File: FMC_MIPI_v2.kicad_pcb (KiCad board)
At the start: 6 copper layers, 69 x 112 mm, 67 parts, among them IC1 ECLAMP2398P.TCT, IC2 AT24MAC402-MAHM-T, J1 ASP-134488-01, J2 QTH-060-01-L-D-A, U2 SN74AVC2T45DCUR, U5 TS3DDR3812_RUA_42, U6 TS3DDR3812_RUA_42, U8 SN74AVCH16T245_DGV_48

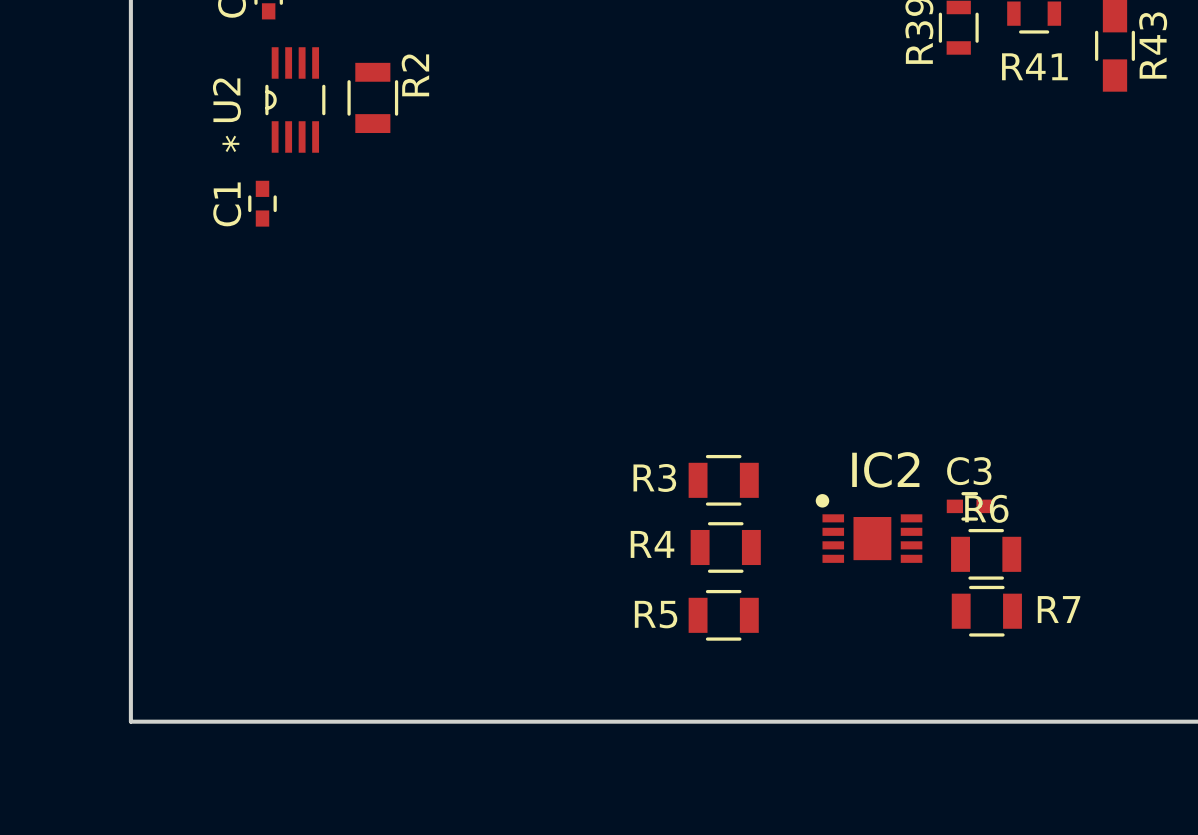
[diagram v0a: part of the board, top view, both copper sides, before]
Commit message: added more level shifters and power 1.8 Volt
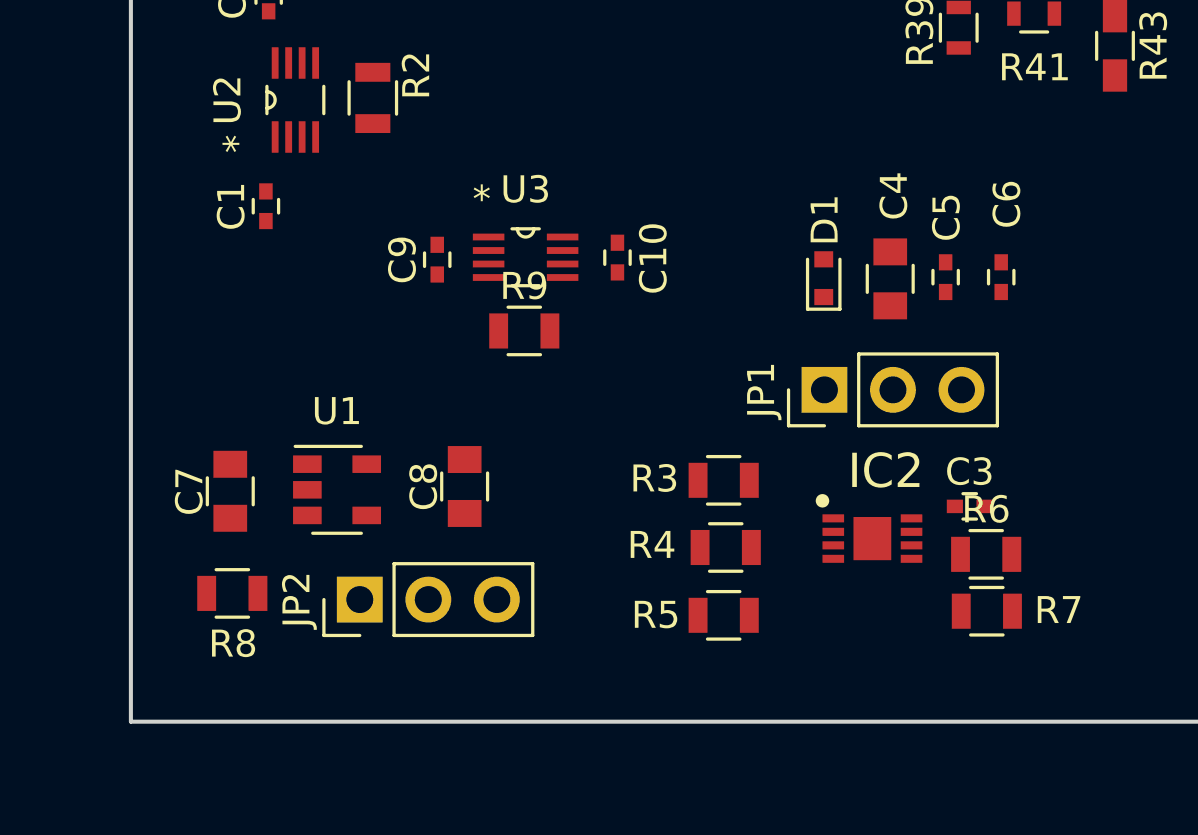
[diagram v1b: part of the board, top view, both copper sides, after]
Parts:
- added C10: 0.1uF, Capacitors_SMD:C_0402, F.Cu at (108.5, 123.8)
- added C4: 4.7uF, Capacitors_SMD:C_0805, F.Cu at (118.6, 124.6)
- added C5: 0.1uF, Capacitors_SMD:C_0402, F.Cu at (120.7, 124.5)
- added C6: 0.1uF, Capacitors_SMD:C_0402, F.Cu at (122.8, 124.5)
- added C7: 1uF, Capacitors_SMD:C_0805, F.Cu at (94.2, 132.5)
- added C8: 1uF, Capacitors_SMD:C_0805, F.Cu at (102.9, 132.3)
- added C9: 0.1uF, Capacitors_SMD:C_0402, F.Cu at (101.9, 123.9)
- added D1: UCLAMP0501H.TCT, Diodes_SMD:D_SOD-523, F.Cu at (116.2, 124.6)
- added JP1: Jumper_3_Bridged12, Pin_Headers:Pin_Header_Straight_1x03_Pitch2.54mm, F.Cu at (116.2, 128.7)
- added JP2: Jumper_3_Bridged12, Pin_Headers:Pin_Header_Straight_1x03_Pitch2.54mm, F.Cu at (99.0, 136.5)
- added R8: 0, Resistors_SMD:R_0805, F.Cu at (94.3, 136.2)
- added R9: 0, Resistors_SMD:R_0805, F.Cu at (105.1, 126.5)
- added U1: LP5907MFX-1.8, TO_SOT_Packages_SMD:SOT-23-5, F.Cu at (98.1, 132.4)
- added U3: SN74AVC2T45DCUR, FMC_MIPI_v2_sym:SN74AVC2T45DCUR, F.Cu at (105.1, 123.8)
- moved C1 0.16 mm to (95.5, 121.9)
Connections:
- IC1 pad 11: (no net) -> V1p8_GPIO9_IN
- IC1 pad 12: (no net) -> V1p8_GPIO17_IN
- J2 pad 102: (no net) -> /Jetson_connector/DVDD_CAM_IO_1V8
- J2 pad 108: (no net) -> /Jetson_connector/JT_VDD_3V3
- J2 pad 109: (no net) -> /Jetson_connector/JT_VDD_5V
- J2 pad 110: (no net) -> /Jetson_connector/JT_VDD_3V3
- J2 pad 118: (no net) -> /Jetson_connector/JT_VDD_5V
- J2 pad 120: (no net) -> /Jetson_connector/JT_VDD_5V

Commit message: minor changes 4
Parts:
- removed IC1: ECLAMP2398P.TCT, SON50P160X400X65-17N
- added C11: 0.1uF, Capacitors_SMD:C_0402, F.Cu at (36.0, 55.1)
- added C12: 0.1uF, Capacitors_SMD:C_0402, F.Cu at (44.7, 55.4)
- added C13: 0.1uF, Capacitors_SMD:C_0402, F.Cu at (47.5, 72.8)
- added C24: 0.1uF, Capacitors_SMD:C_0402, F.Cu at (47.4, 68.4)
- added IC3: TCA9406DCUR, FMC_MIPI_v2_sym:SOP50P310X90-8N, F.Cu at (40.5, 55.4)
- added R10: 4.7k, Resistors_SMD:R_0805, F.Cu at (116.9, 67.3)
- added R11: 4.7k, Resistors_SMD:R_0805, F.Cu at (35.5, 66.0)
- added R12: 0, Resistors_SMD:R_0805, F.Cu at (44.8, 57.6)
- added R13: 0, Resistors_SMD:R_0805, F.Cu at (35.9, 57.2)
- added R14: 0, Resistors_SMD:R_0805, F.Cu at (44.6, 52.4)
- added R15: 0, Resistors_SMD:R_0805, F.Cu at (36.0, 52.9)
- R2, R9: value 0 -> 4.7k
- U3: value SN74AVC2T45DCUR -> SN74AVCH16T245_DGV_48; footprint FMC_MIPI_v2_sym:SN74AVC2T45DCUR -> FMC_MIPI_v2_sym:DGV48
- moved C10 88.5 mm to (36.2, 72.9), turned to 180 degrees
- moved C9 86.2 mm to (35.8, 68.5), turned to 180 degrees
- moved R9 85.6 mm to (35.6, 76.5), turned to 180 degrees
- moved U3 82.7 mm to (41.7, 70.6)
- moved R2 0.40 mm to (99.7, 117.6)
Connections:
- C10 pad 1: Earth -> /Slow_signals_level_shifters/VDD_VADJ
- C10 pad 2: /LVDS_to_Jetson_lines/VOLT_1P8 -> Earth
- C9 pad 1: Earth -> /Slow_signals_level_shifters/VDD_VADJ
- C9 pad 2: /LVDS_to_Jetson_lines/VDD_VADJ -> Earth
- J2 pad 112: /Jetson_connector/JT_1p8V_GPIO9_IN -> JT_1p8V_GPIO9_IN
- J2 pad 117: /Jetson_connector/JT_1p8V_GPIO17_IN -> JT_1p8V_GPIO17_IN
- J2 pad 75: /Jetson_connector/JT_1p8V_I2C_CAM_CLK -> JT_1p8V_I2C_CAM_CLK
- J2 pad 77: /Jetson_connector/JT_1p8V_I2C_CAM_DAT -> JT_1p8V_I2C_CAM_DAT
- J2 pad 91: /Jetson_connector/JT_1p8V_CAM0_MCLK -> JT_1p8V_CAM0_MCLK
- J2 pad 93: /Jetson_connector/JT_1p8V_CAM0_PWR -> JT_1p8V_CAM0_PWR
- J2 pad 95: /Jetson_connector/JT_1p8V_CAM0_RST -> JT_1p8V_CAM0_RST
- R2 pad 2: /LVDS_to_Jetson_lines/DIR -> /LVDS_to_Jetson_lines/DIR_U2
- R6 pad 2: /Jetson_connector/V1p8_I2C_CAM_CLK -> (no net)
- R7 pad 2: /Jetson_connector/V1p8_I2C_CAM_DAT -> (no net)
- R9 pad 1: /LVDS_to_Jetson_lines/VDD_VADJ -> /Slow_signals_level_shifters/2DIR_U3
- R9 pad 2: /LVDS_to_Jetson_lines/DIR -> /Slow_signals_level_shifters/VOLT_1P8
- U2 pad 5: /LVDS_to_Jetson_lines/DIR -> /LVDS_to_Jetson_lines/DIR_U2
- U3 pad 1: /LVDS_to_Jetson_lines/VDD_VADJ -> /Slow_signals_level_shifters/1DIR_U3
- U3 pad 5: /LVDS_to_Jetson_lines/DIR -> (no net)
- U3 pad 6: V1p8_GPIO9_IN -> (no net)
- U3 pad 7: V1p8_GPIO17_IN -> /Slow_signals_level_shifters/VDD_VADJ
- U3 pad 8: /LVDS_to_Jetson_lines/VOLT_1P8 -> (no net)
- U8 pad 1: Earth -> /LVDS_to_Jetson_lines/DIR_U8
- U8 pad 24: Earth -> /LVDS_to_Jetson_lines/DIR_U8
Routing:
- net JT_1p8V_I2C_CAM_DAT: track 0.00 -> 16.5 mm, vias 0 -> 2
- net /Jetson_connector/JT_1p8V_I2C_CAM_DAT: track 16.5 -> 0.00 mm, vias 2 -> 0
- net JT_1p8V_GPIO9_IN: track 0.00 -> 13.4 mm
- net /Jetson_connector/JT_1p8V_GPIO9_IN: track 13.4 -> 0.00 mm
- net JT_1p8V_I2C_CAM_CLK: track 0.00 -> 10.9 mm
- net /Jetson_connector/JT_1p8V_I2C_CAM_CLK: track 10.9 -> 0.00 mm
- net JT_1p8V_CAM0_MCLK: track 0.00 -> 9.35 mm, vias 0 -> 2
- net /Jetson_connector/JT_1p8V_CAM0_MCLK: track 9.35 -> 0.00 mm, vias 2 -> 0
- net JT_1p8V_CAM0_PWR: track 0.00 -> 6.31 mm
- net /Jetson_connector/JT_1p8V_CAM0_PWR: track 6.31 -> 0.00 mm
- net JT_1p8V_CAM0_RST: track 0.00 -> 6.18 mm
- net /Jetson_connector/JT_1p8V_CAM0_RST: track 6.18 -> 0.00 mm
- net JT_1p8V_GPIO17_IN: track 0.00 -> 5.35 mm
- net /Jetson_connector/JT_1p8V_GPIO17_IN: track 5.35 -> 0.00 mm

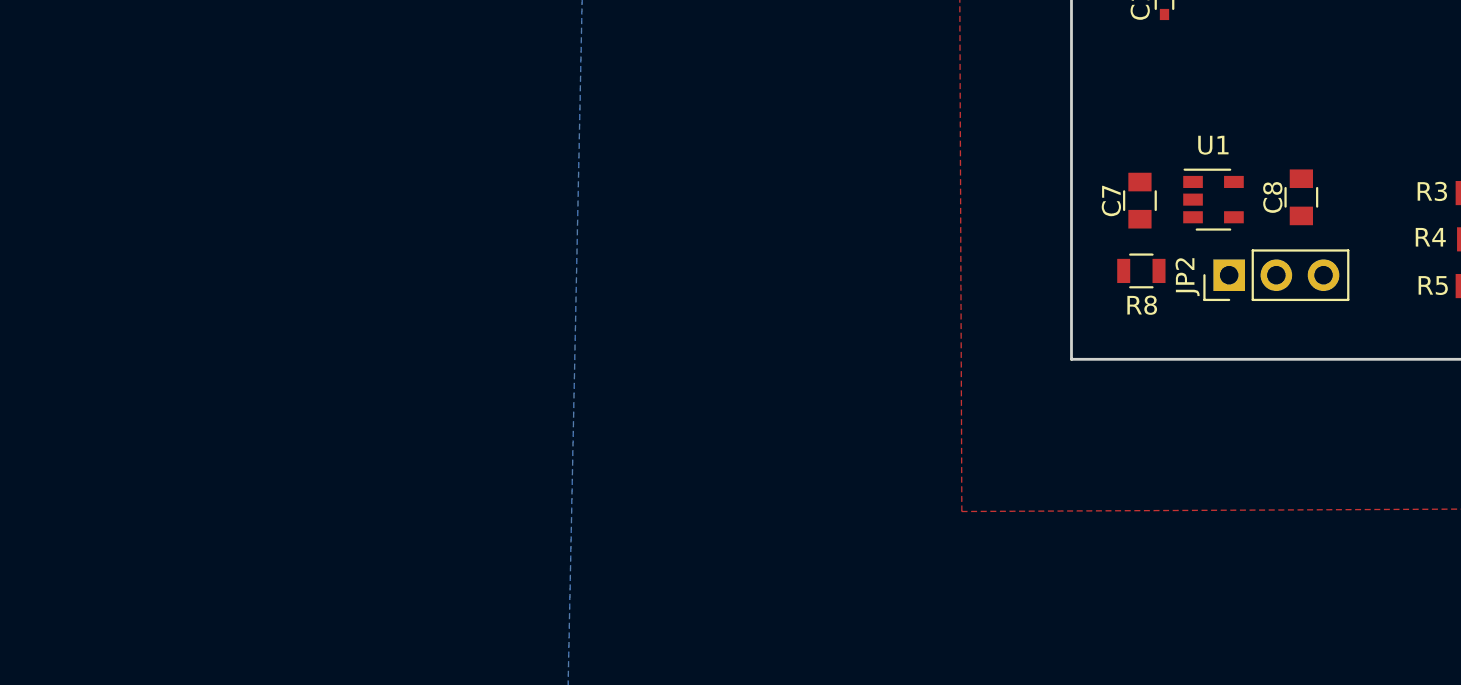
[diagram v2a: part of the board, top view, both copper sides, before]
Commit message: adding more power supplies
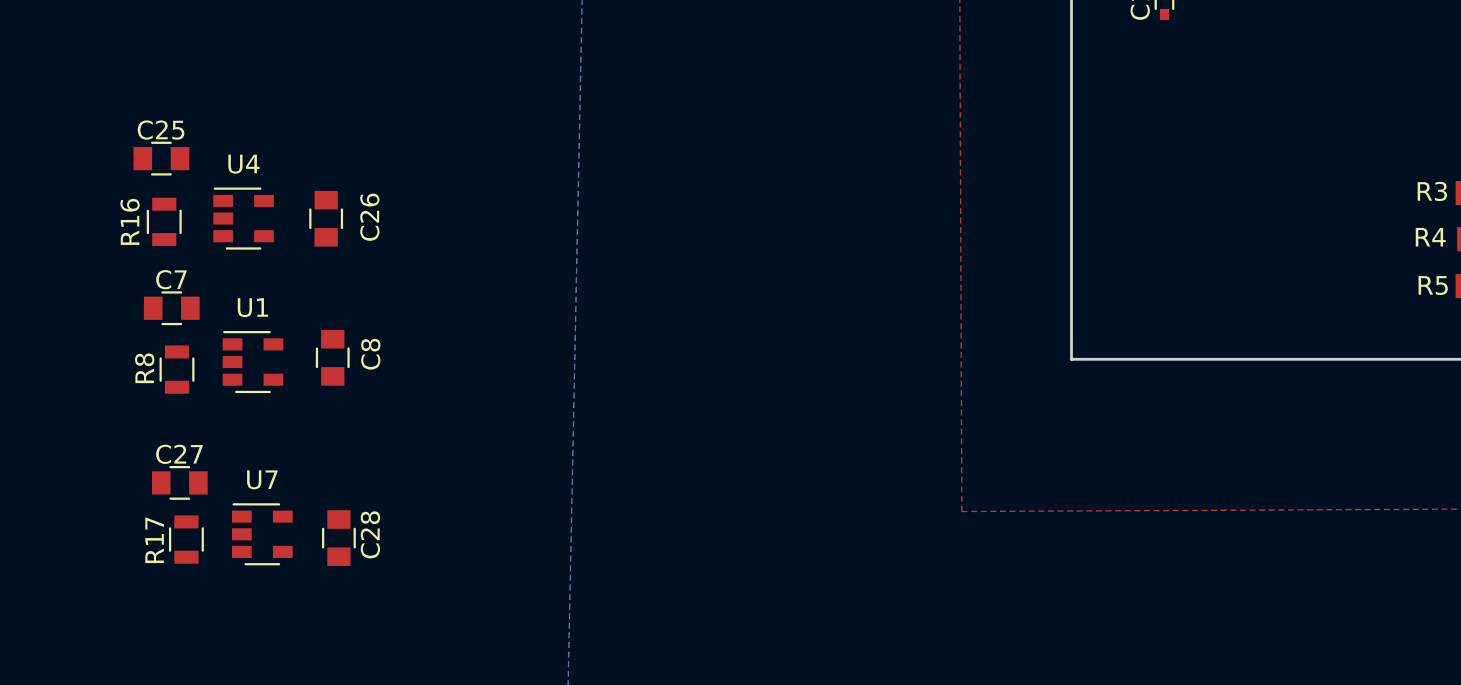
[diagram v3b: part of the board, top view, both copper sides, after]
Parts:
- removed JP2: Jumper_3_Bridged12, Pin_Headers:Pin_Header_Straight_1x03_Pitch2.54mm
- added C25: 1uF, Capacitors_SMD:C_0805, F.Cu at (41.5, 130.2)
- added C26: 1uF, Capacitors_SMD:C_0805, F.Cu at (50.4, 133.4)
- added C27: 1uF, Capacitors_SMD:C_0805, F.Cu at (42.5, 147.7)
- added C28: 1uF, Capacitors_SMD:C_0805, F.Cu at (51.1, 150.6)
- added R16: 0, Resistors_SMD:R_0805, F.Cu at (41.7, 133.6)
- added R17: 0, Resistors_SMD:R_0805, F.Cu at (42.9, 150.7)
- added U4: TLV75525PDBV, TO_SOT_Packages_SMD:SOT-23-5, F.Cu at (45.9, 133.4)
- added U7: LP5907MFX-1.2, TO_SOT_Packages_SMD:SOT-23-5, F.Cu at (47.0, 150.4)
- moved C8 52.8 mm to (50.7, 140.9)
- moved U1 52.4 mm to (46.5, 141.1)
- moved C7 52.4 mm to (42.1, 138.3), turned to 0 degrees
- moved R8 52.2 mm to (42.4, 141.6), turned to 270 degrees
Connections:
- net /Jetson_connector/VDD_CAM_1V8_CAM renamed /Jetson_connector/VCC_1V8_EEPROM
- net /LVDS_to_Jetson_lines/VOLT_1P2 renamed /VOLT_1P2
- net /LVDS_to_Jetson_lines/VOLT_2P5 renamed /VOLT_2P5
- C1 pad 2: /LVDS_to_Jetson_lines/VDD_VADJ -> /VDD_VADJ
- C10 pad 1: /Slow_signals_level_shifters/VDD_VADJ -> /VDD_VADJ
- C11 pad 1: /Slow_signals_level_shifters/VOLT_1P8 -> /VOLT_1P8
- C12 pad 1: /Slow_signals_level_shifters/VDD_VADJ -> /VDD_VADJ
- C13 pad 1: /Slow_signals_level_shifters/VOLT_1P8 -> /VOLT_1P8
- C14 pad 1: /LVDS_to_Jetson_lines/VDD_VADJ -> /VDD_VADJ
- C15 pad 1: /LVDS_to_Jetson_lines/VDD_VADJ -> /VDD_VADJ
- C18 pad 2: /LVDS_to_Jetson_lines/VOLT_3P3 -> /VOLT_3P3
- C19 pad 2: /LVDS_to_Jetson_lines/VOLT_3P3 -> /VOLT_3P3
- C2 pad 2: /LVDS_to_Jetson_lines/VOLT_3P3 -> /VOLT_3P3
- C20 pad 2: /LVDS_to_Jetson_lines/VOLT_3P3 -> /VOLT_3P3
- C21 pad 2: /LVDS_to_Jetson_lines/VOLT_3P3 -> /VOLT_3P3
- C22 pad 2: /LVDS_to_Jetson_lines/VOLT_3P3 -> /VOLT_3P3
- C23 pad 2: /LVDS_to_Jetson_lines/VOLT_3P3 -> /VOLT_3P3
- C24 pad 1: /Slow_signals_level_shifters/VOLT_1P8 -> /VOLT_1P8
- C7 pad 2: /Jetson_connector/JT_VDD_5V -> /VOLT_3P3
- C8 pad 2: /Jetson_connector/LDO_1V8 -> /VOLT_1P8
- C9 pad 1: /Slow_signals_level_shifters/VDD_VADJ -> /VDD_VADJ
- IC3 pad 3: /Slow_signals_level_shifters/VOLT_1P8 -> /VOLT_1P8
- IC3 pad 6: /Slow_signals_level_shifters/VOLT_1P8 -> /VOLT_1P8
- IC3 pad 7: /Slow_signals_level_shifters/VDD_VADJ -> /VDD_VADJ
- JP1 pad 1: (no net) -> /VOLT_1P8
- JP1 pad 3: /Jetson_connector/JETSON_1V8 -> /Jetson_connector/DVDD_CAM_IO_1V8
- R2 pad 1: /LVDS_to_Jetson_lines/VDD_VADJ -> /VDD_VADJ
- R37 pad 2: /LVDS_to_Jetson_lines/VOLT_3P3 -> /VOLT_3P3
- R38 pad 2: /LVDS_to_Jetson_lines/VOLT_3P3 -> /VOLT_3P3
- R6 pad 2: (no net) -> JT_1p8V_I2C_CAM_CLK
- R7 pad 2: (no net) -> JT_1p8V_I2C_CAM_DAT
- R8 pad 1: /Jetson_connector/JT_VDD_5V -> /VOLT_3P3
- R9 pad 2: /Slow_signals_level_shifters/VOLT_1P8 -> /VOLT_1P8
- U1 pad 1: /Jetson_connector/JT_VDD_5V -> /VOLT_3P3
- U1 pad 5: /Jetson_connector/LDO_1V8 -> /VOLT_1P8
- U2 pad 1: /LVDS_to_Jetson_lines/VDD_VADJ -> /VDD_VADJ
- U2 pad 8: /LVDS_to_Jetson_lines/VOLT_3P3 -> /VOLT_3P3
- U3 pad 18: /Slow_signals_level_shifters/VDD_VADJ -> /VDD_VADJ
- U3 pad 31: /Slow_signals_level_shifters/VOLT_1P8 -> /VOLT_1P8
- U3 pad 42: /Slow_signals_level_shifters/VOLT_1P8 -> /VOLT_1P8
- U3 pad 7: /Slow_signals_level_shifters/VDD_VADJ -> /VDD_VADJ
- U5 pad 1: /LVDS_to_Jetson_lines/VOLT_3P3 -> /VOLT_3P3
- U5 pad 17: /LVDS_to_Jetson_lines/VOLT_3P3 -> /VOLT_3P3
- U5 pad 30: /LVDS_to_Jetson_lines/VOLT_3P3 -> /VOLT_3P3
- U6 pad 1: /LVDS_to_Jetson_lines/VOLT_3P3 -> /VOLT_3P3
- U6 pad 17: /LVDS_to_Jetson_lines/VOLT_3P3 -> /VOLT_3P3
- U6 pad 30: /LVDS_to_Jetson_lines/VOLT_3P3 -> /VOLT_3P3
- U8 pad 18: /LVDS_to_Jetson_lines/VDD_VADJ -> /VDD_VADJ
- U8 pad 7: /LVDS_to_Jetson_lines/VDD_VADJ -> /VDD_VADJ

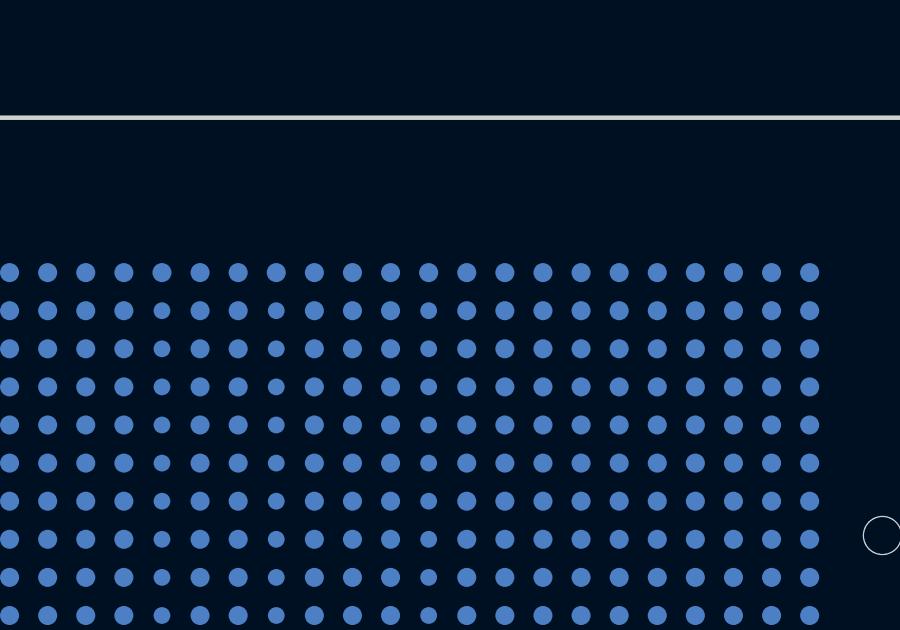
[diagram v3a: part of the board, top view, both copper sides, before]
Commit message: populating FMC connector
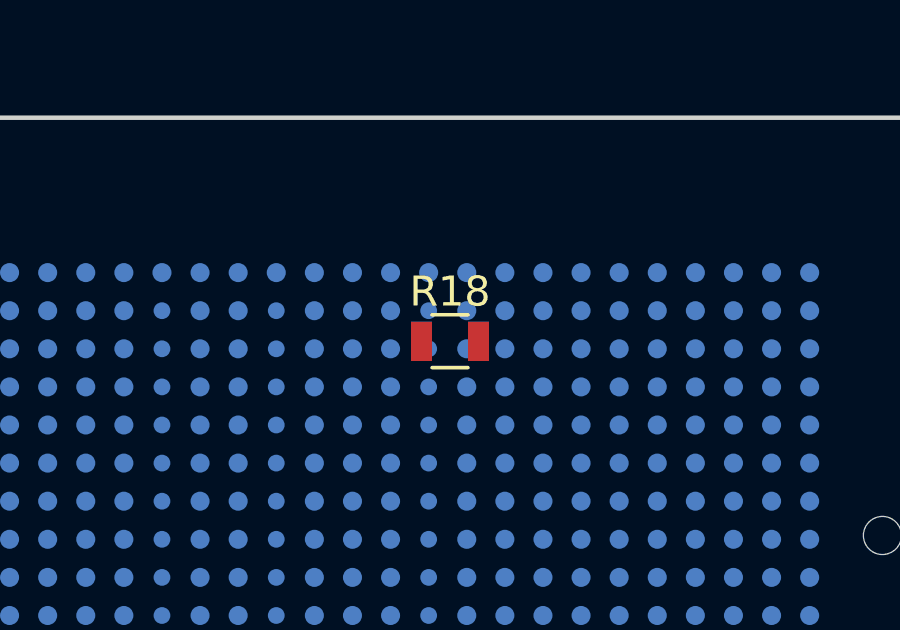
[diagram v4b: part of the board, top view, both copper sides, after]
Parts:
- added R18: 0, Resistors_SMD:R_0805, F.Cu at (137.7, 36.4)
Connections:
- J1 pad C39: (no net) -> /VOLT_3P3
- J1 pad D30: (no net) -> /FMC_Connector/TDI
- J1 pad D31: (no net) -> /FMC_Connector/TDO
- J1 pad D36: (no net) -> /VOLT_3P3
- J1 pad D38: (no net) -> /VOLT_3P3
- J1 pad D40: (no net) -> /VOLT_3P3
- J1 pad E39: (no net) -> /VDD_VADJ
- J1 pad F40: (no net) -> /VDD_VADJ
- J1 pad G39: (no net) -> /VDD_VADJ
- J1 pad H40: (no net) -> /VDD_VADJ

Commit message: cleanup 3D shapes
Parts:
- moved C10 76.6 mm to (21.5, 148.0)
- moved C11 76.6 mm to (21.3, 130.3)
- moved R12 76.6 mm to (30.1, 132.7)
- moved R13 76.6 mm to (21.2, 132.3)
- moved C13 76.6 mm to (32.8, 148.0)
- moved R14 76.6 mm to (29.9, 127.5)
- moved R15 76.6 mm to (21.3, 128.0)
- moved R9 76.6 mm to (20.9, 151.7)
- moved U3 76.6 mm to (27.0, 145.7)
- moved C12 76.6 mm to (30.0, 130.5)
- moved C24 76.6 mm to (32.7, 143.5)
- moved C9 76.6 mm to (21.1, 143.6)
- moved IC3 76.6 mm to (25.8, 130.5)
- moved R11 76.6 mm to (20.8, 141.1)

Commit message: Adding more LVDS lines
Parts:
- moved C28 211.6 mm to (262.7, 153.5)
- moved C8 211.6 mm to (262.3, 143.8)
- moved IC3 211.6 mm to (237.4, 133.4)
- moved C10 211.6 mm to (233.0, 151.0)
- moved C11 211.6 mm to (232.9, 133.2)
- moved C12 211.6 mm to (241.6, 133.5)
- moved C13 211.6 mm to (244.4, 150.9)
- moved C24 211.6 mm to (244.2, 146.4)
- moved C25 211.6 mm to (253.1, 133.1)
- moved C26 211.6 mm to (262.0, 136.4)
- moved C27 211.6 mm to (254.1, 150.6)
- moved C7 211.6 mm to (253.7, 141.2)
- moved C9 211.6 mm to (232.7, 146.5)
- moved R11 211.6 mm to (232.4, 144.1)
- moved R12 211.6 mm to (241.7, 135.6)
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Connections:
- net /Jetson_connector/DVDD_CAM_IO_1V8 renamed /Jetson_connector/JT_VDD_1V8
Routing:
- net JT_1p8V_I2C_CAM_DAT: track 16.5 -> 0.00 mm, vias 2 -> 0
- net JT_1p8V_GPIO9_IN: track 13.4 -> 0.00 mm
- net JT_1p8V_I2C_CAM_CLK: track 10.9 -> 0.00 mm
- net JT_1p8V_CAM0_MCLK: track 9.35 -> 0.00 mm, vias 2 -> 0
- net JT_1p8V_CAM0_PWR: track 6.31 -> 0.00 mm
- net JT_1p8V_CAM0_RST: track 6.18 -> 0.00 mm
- net JT_1p8V_GPIO17_IN: track 5.35 -> 0.00 mm
